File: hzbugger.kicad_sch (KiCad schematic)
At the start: 59 parts, among them J2 IDC, J3 BOOT0-HDR, J4 SWD, J5 DC, J6 GPIO, J7 SWDOUT_HDR, U1 STM32F103C8T6, U2 SRV05-4, U3 AMS1117-3.3, U4 HX AM 90D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

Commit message: other model, reset sw now in place
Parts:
- removed J3: BOOT0-HDR, Connector_PinHeader_2.54mm:PinHeader_1x03_P2.54mm_Vertical, symbol Connector:Conn_01x03_Pin
- removed TP2: NRST, TestPoint:TestPoint_Pad_D2.0mm, symbol Connector:TestPoint
- added SW1: RESET_SW, hzbugger:SW-SMD_4P-L5.1-W5.1-P3.70-LS6.5-TL_H1.5, symbol hzbugger:TS-1187A-B-A-B
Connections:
- net +3V3: now also R7.2
- net GND: now also R8.2, SW1.3 (C), SW1.4 (D)
- net at R7.1: now also C17.2, U1.7 (NRST), SW1.1 (A), SW1.2 (B)
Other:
- note added: "HZBUGGER rev.A"
- note removed: "RESET-NAPPI! BOOT-nappi?"
- moved on the sheet: R7, R8

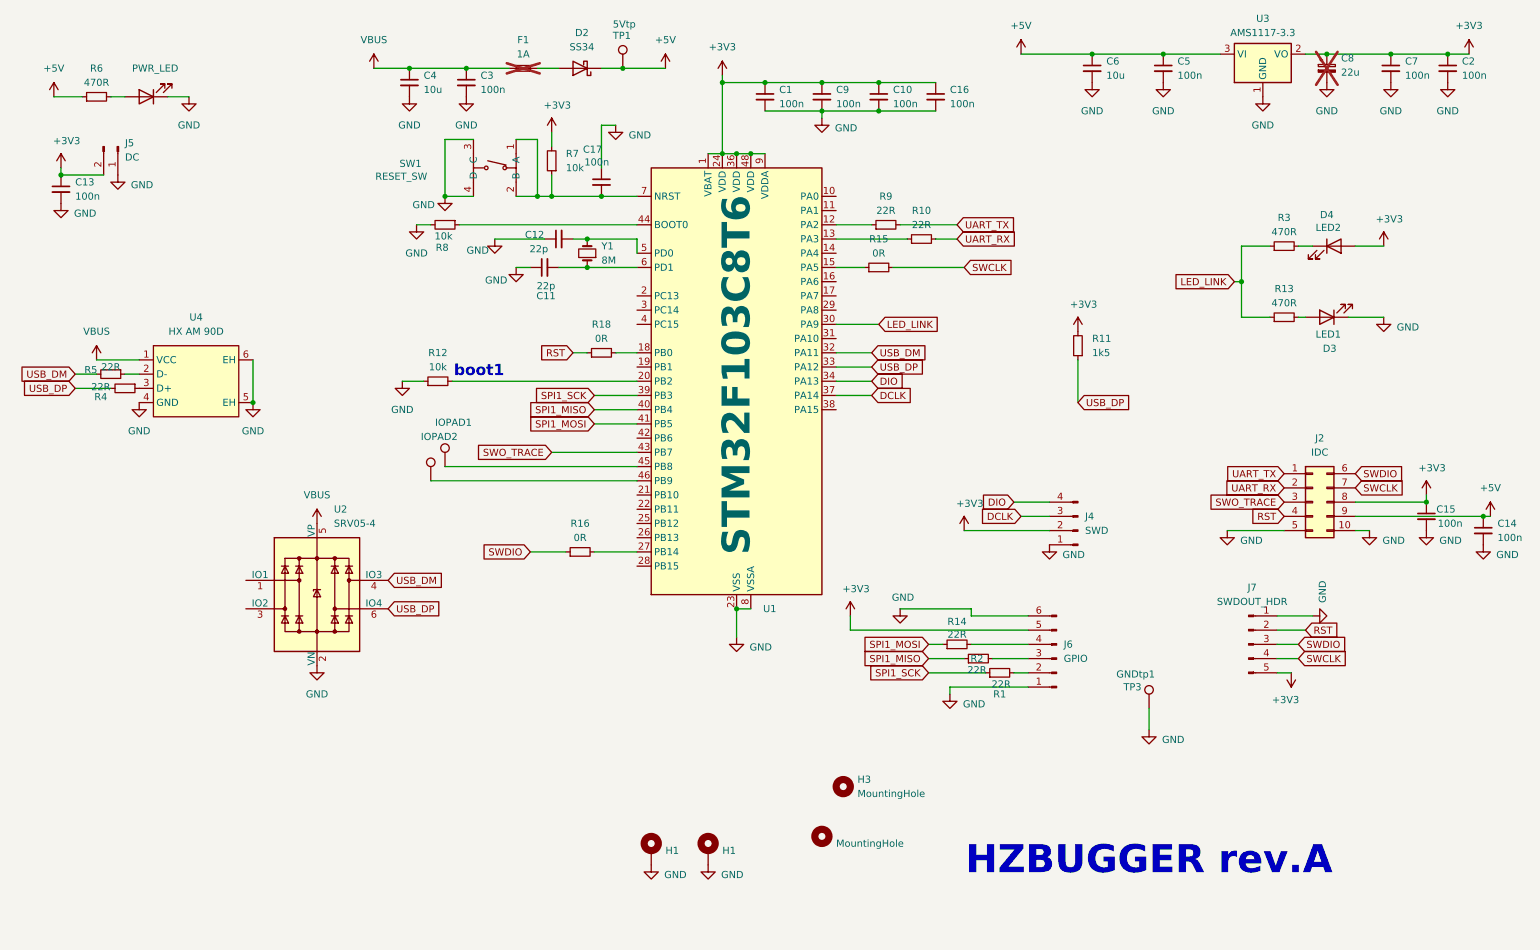
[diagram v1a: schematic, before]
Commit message: change xtal package etc
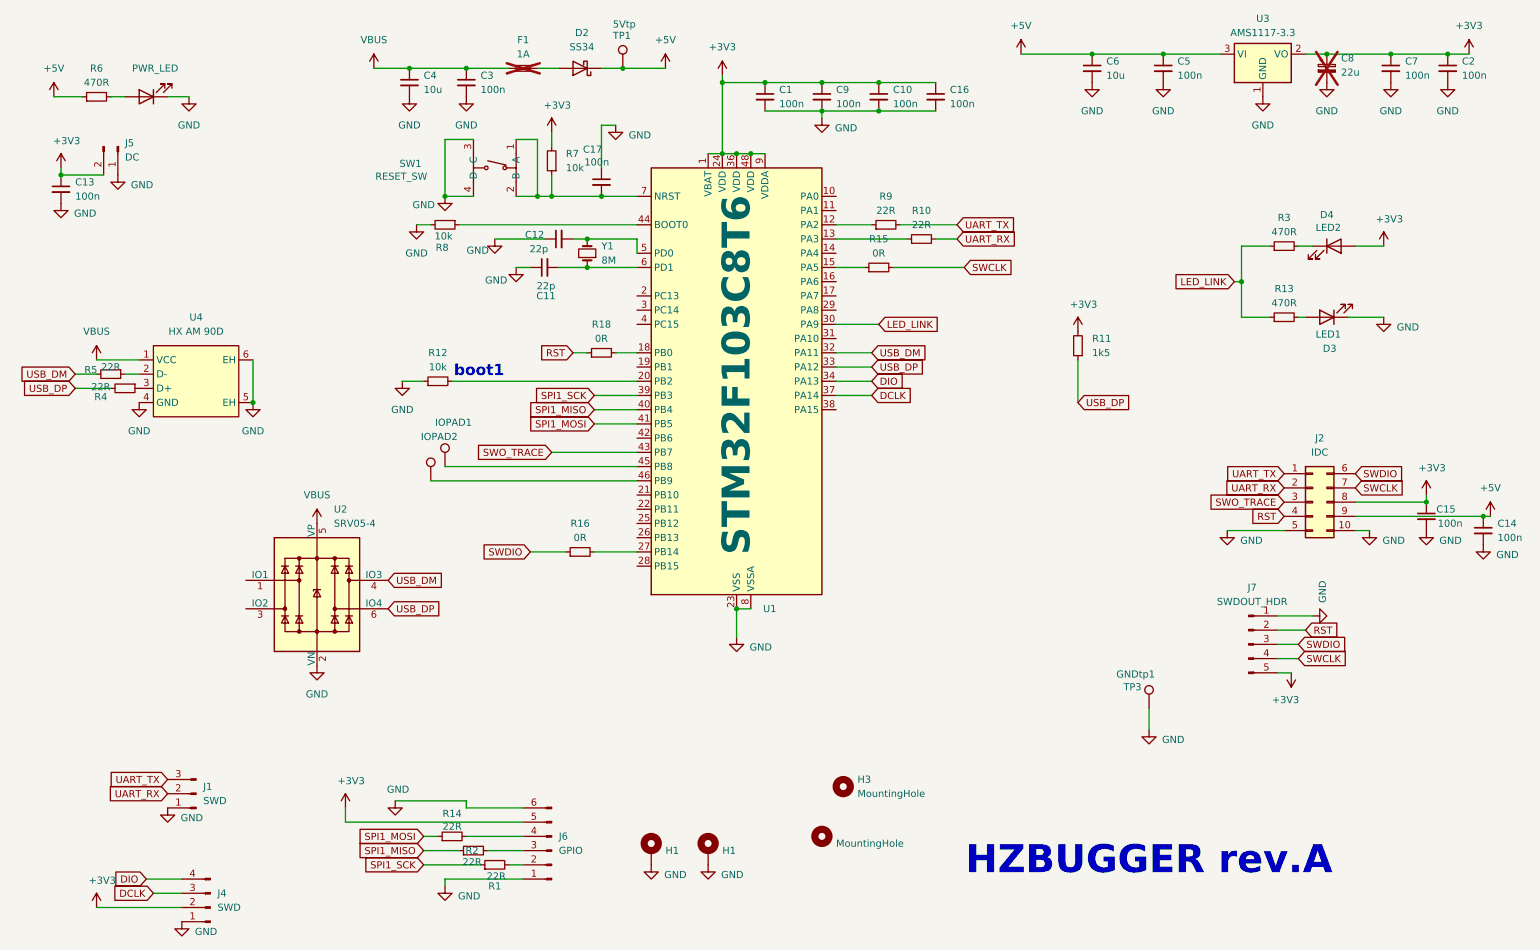
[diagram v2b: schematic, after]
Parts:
- added J1: SWD, Connector_PinHeader_2.54mm:PinHeader_1x03_P2.54mm_Vertical, symbol Connector:Conn_01x03_Pin
- Y1: footprint Crystal:Crystal_SMD_HC49-SD -> Crystal:Crystal_SMD_5032-2Pin_5.0x3.2mm; LCSC C12674 -> C115962
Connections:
- net GND: now also J1.1 (Pin_1)
- net UART_RX: now also J1.2 (Pin_2)
- net UART_TX: now also J1.3 (Pin_3)
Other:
- moved on the sheet: J4, J6, R1, R14, R2

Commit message: sw lcsc etc
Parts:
- SW1: LCSC (none) -> C318884; LCSC Part C318884 -> (none)
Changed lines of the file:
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@@
 			)
 		)
-		(property "LCSC Part" "C318884"
+		(property "LCSC" "C318884"
 			(at 82.55 50.8 0)
 			(effects

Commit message: remove pinhead, just idc left
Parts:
- removed C1, C13: 100n, Capacitor_SMD:C_0603_1608Metric, symbol Device:C_Small
- removed H3, H4: MountingHole, MountingHole:MountingHole_3.2mm_M3_Pad_TopBottom, symbol Mechanical:MountingHole
- removed J1: SWD, Connector_PinHeader_2.54mm:PinHeader_1x03_P2.54mm_Vertical, symbol Connector:Conn_01x03_Pin
- removed J5: DC, Connector_PinHeader_2.54mm:PinHeader_1x02_P2.54mm_Vertical, symbol Connector:Conn_01x02_Pin
- removed J7: SWDOUT_HDR, Connector_PinHeader_2.54mm:PinHeader_1x05_P2.54mm_Horizontal, symbol Connector:Conn_01x05_Pin
- removed R18: 0R, Resistor_SMD:R_0603_1608Metric_Pad0.98x0.95mm_HandSolder, symbol Device:R_Small
- removed TP3: GNDtp1, TestPoint:TestPoint_Loop_D1.80mm_Drill1.0mm_Beaded, symbol Connector:TestPoint
- added R17: 22R, Resistor_SMD:R_0402_1005Metric, symbol Device:R_Small
- D1, D3, D4: footprint LED_THT:LED_D3.0mm -> LED_SMD:LED_0603_1608Metric
- R1, R14, R2, R9: footprint Resistor_SMD:R_0603_1608Metric -> Resistor_SMD:R_0402_1005Metric; LCSC C23345 -> C25092
- R10: footprint Resistor_SMD:R_0603_1608Metric_Pad0.98x0.95mm_HandSolder -> Resistor_SMD:R_0402_1005Metric; LCSC C23345 -> C25092
- R12, R7, R8: footprint Resistor_SMD:R_0603_1608Metric -> Resistor_SMD:R_0402_1005Metric; LCSC C25804 -> C25744
- R13, R3, R6: value 470R -> 1k5; LCSC C23179 -> (none)
- R15: value 0R -> 22R; footprint Resistor_SMD:R_0603_1608Metric_Pad0.98x0.95mm_HandSolder -> Resistor_SMD:R_0402_1005Metric; LCSC C21189 -> C25092
- R16: value 0R -> 22R; footprint Resistor_SMD:R_0603_1608Metric -> Resistor_SMD:R_0402_1005Metric; LCSC C21189 -> C25092
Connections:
- net +3V3: now also R6.1
- net +5V: no longer R6.1
- net RST: now also R17.1
- net at U1.18 (PB0): now also R17.2
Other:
- note added: "PINOUT TO SILK!"
- note added: "UART TX & RX LEDs?"
- moved on the sheet: C14, C15, J2, R6

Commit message: layout further
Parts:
- removed H1, H2: H1, MountingHole:MountingHole_3.2mm_M3_DIN965_Pad_TopBottom, symbol Mechanical:MountingHole_Pad
- removed TP4: IOPAD1, TestPoint:TestPoint_Pad_D1.0mm, symbol Connector:TestPoint
- removed TP5: IOPAD2, TestPoint:TestPoint_Pad_D1.0mm, symbol Connector:TestPoint
- added D5: LED1, LED_SMD:LED_0603_1608Metric, symbol Device:LED
- added R18: 1k5, Resistor_SMD:R_0402_1005Metric, symbol Device:R_Small
- added TP2: TPG1, TestPoint:TestPoint_Pad_D1.0mm, symbol Connector:TestPoint
- C8: value 22u -> 100u; footprint Capacitor_Tantalum_SMD:CP_EIA-6032-15_Kemet-U_Pad2.25x2.35mm_HandSolder -> Capacitor_Tantalum_SMD:CP_EIA-3528-21_Kemet-B_Pad1.50x2.35mm_HandSolder; LCSC DNP -> C16133; now fitted
- J4: footprint Connector_PinHeader_2.54mm:PinHeader_1x04_P2.54mm_Vertical -> hzbugger:SMD-PinHeader_1x04_P2.54mm_Vertical
- J6: footprint Connector_PinHeader_2.54mm:PinHeader_1x06_P2.54mm_Vertical -> hzbugger:SMD-PinHeader_1x06_P2.54mm_Vertical
- R11, R13, R3: footprint Resistor_SMD:R_0603_1608Metric -> Resistor_SMD:R_0402_1005Metric
- TP1: value 5Vtp -> TPA14; footprint TestPoint:TestPoint_Pad_D2.0mm -> TestPoint:TestPoint_Pad_D1.0mm
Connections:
- net +5V: no longer TP1.1
- net GND: now also D5.1 (K), TP2.1
- net USB_DM: now also U2.1 (IO1); no longer U2.4 (IO3)
- net at U1.14 (PA4): now also TP1.1
- net at U1.29 (PA8): now also R18.1
- new net: D5.2 (A), R18.2
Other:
- note removed: "PINOUT TO SILK!"

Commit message: w.i.p
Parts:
- J2: footprint Connector_IDC:IDC-Header_2x05_P2.54mm_Vertical -> hzbugger:SMD-pcbend-IDC-Header_2x05_P2.54mm
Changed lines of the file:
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@@
 			)
 		)
-		(property "Footprint" "Connector_IDC:IDC-Header_2x05_P2.54mm_Vertical"
+		(property "Footprint" "hzbugger:SMD-pcbend-IDC-Header_2x05_P2.54mm"
 			(at 196.85 134.62 0)
 			(effects

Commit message: IDC
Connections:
- net +3V3: now also J2.10 (Pin_10); no longer J2.8 (Pin_8)
- net +5V: now also J2.2 (Pin_2); no longer J2.9 (Pin_9)
- net GND: now also J2.6 (Pin_6); no longer J2.10 (Pin_10)
- net SWDIO: now also J2.9 (Pin_9); no longer J2.6 (Pin_6)
- net SWO_TRACE: now also J2.8 (Pin_8); no longer J2.3 (Pin_3)
- net UART_RX: now also J2.1 (Pin_1); no longer J2.2 (Pin_2)
- net UART_TX: now also J2.3 (Pin_3); no longer J2.1 (Pin_1)
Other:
- moved on the sheet: C14, C15

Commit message: routing
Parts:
- added SW2: BOOT0_SW, hzbugger:SW-SMD_4P-L5.1-W5.1-P3.70-LS6.5-TL_H1.5, symbol hzbugger:TS-1187A-B-A-B
- J6: footprint hzbugger:SMD-PinHeader_1x06_P2.54mm_Vertical -> Connector_PinHeader_2.54mm:PinHeader_1x06_P2.54mm_Vertical
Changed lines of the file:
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@@
 			)
 		)
-		(property "Footprint" "hzbugger:SMD-PinHeader_1x06_P2.54mm_Vertical"
+		(property "Footprint" "Connector_PinHeader_2.54mm:PinHeader_1x06_P2.54mm_Vertical"
 			(at 109.22 172.72 0)
 			(effects
@@
 					(unit 1)
 				)
+			)
+		)
+	)
+	(symbol
+		(lib_id "hzbugger:TS-1187A-B-A-B")
+		(at 66.04 58.42 270)
+		(unit 1)
+		(exclude_from_sim no)
+		(in_bom yes)
+		(on_board yes)
+		(dnp no)
+		(property "Reference" "SW2"
+			(at 47.752 57.658 90)
+			(effects
+				(font
+					(size 1.27 1.27)
+				)
+				(justify left)
+			)
+		)
+		(property "Value" "BOOT0_SW"
+			(at 43.434 59.944 90)
+			(effects
+				(font
+					(size 1.27 1.27)
+				)
+				(justify left)
+			)
+		)
+		(property "Footprint" "hzbugger:SW-SMD_4P-L5.1-W5.1-P3.70-LS6.5-TL_H1.5"
+			(at 53.34 58.42 0)
+			(effects
+				(font
+					(size 1.27 1.27)
+				)
+				(hide yes)
+			)
+		)
+		(property "Datasheet" "https://lcsc.com/product-detail/Tactile-Switches_XKB-Enterprise-TS-1187-B-A-A_C318884.html"
+			(at 50.8 58.42 0)
+			(effects
+				(font
+					(size 1.27 1.27)
+				)
+				(hide yes)
+			)
+		)
+		(property "Description" ""
+			(at 66.04 58.42 0)
+			(effects
+				(font
+					(size 1.27 1.27)
+				)
+				(hide yes)
+			)
+		)
+		(property "LCSC" "C318884"
+			(at 48.26 58.42 0)
+			(effects
+				(font
+					(size 1.27 1.27)
+				)
+				(hide yes)
+			)
+		)
+		(pin "1"
+		)
+		(pin "2"
+		)
+		(pin "3"
+		)
+		(pin "4"
+		)
+		(instances
+			(project "hzbugger"
+				(path "/493ccddd-ac13-43bb-97a7-ed9a2ed970cc"
+					(reference "SW2")
+					(unit 1)
+				)
